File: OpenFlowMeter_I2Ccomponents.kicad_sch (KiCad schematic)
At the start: 7 parts, among them U7 24LC64, U9 TMP100

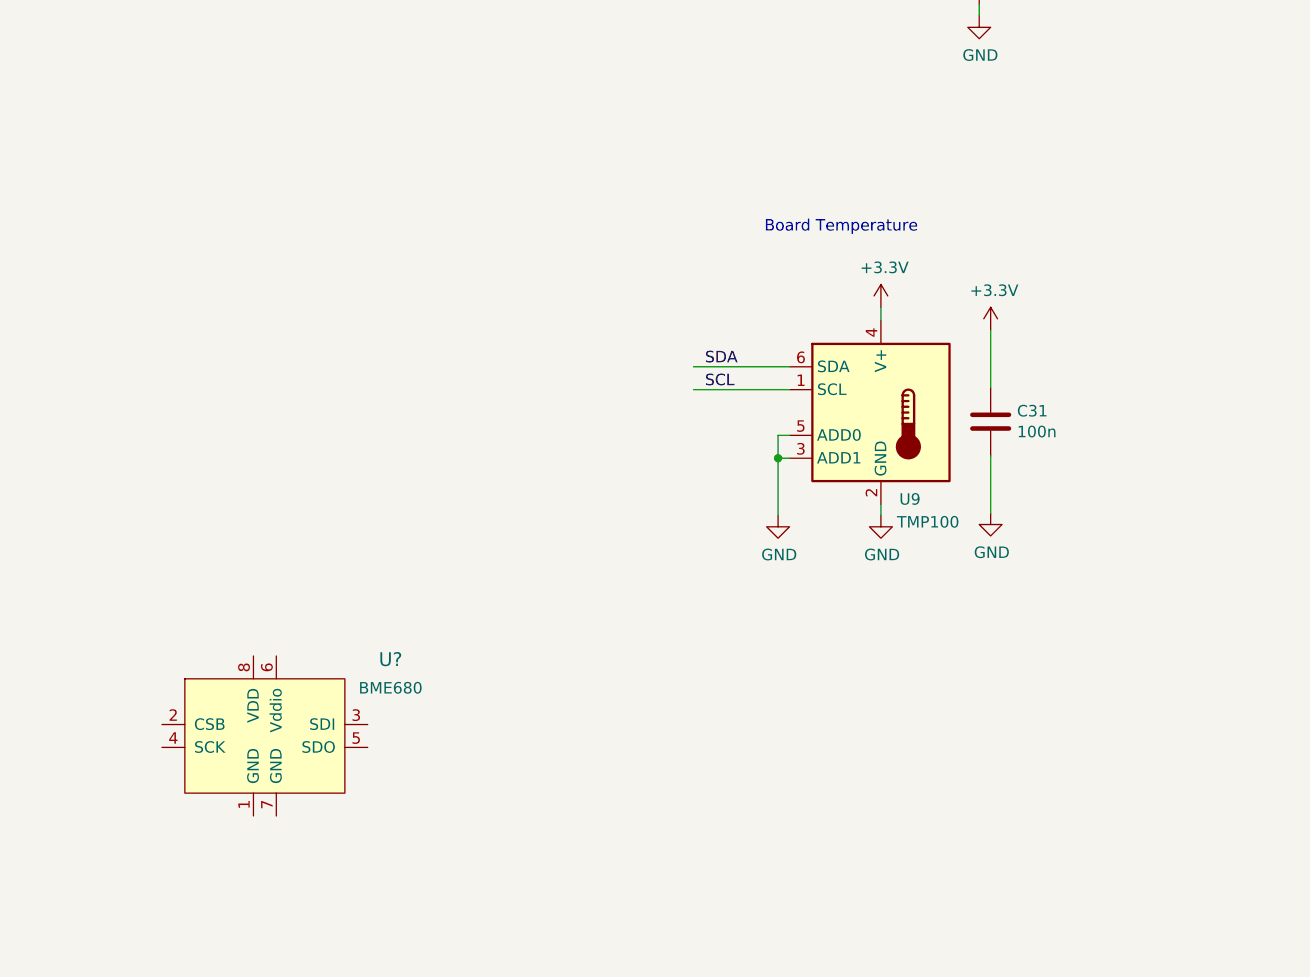
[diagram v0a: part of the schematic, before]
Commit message: added BME680 I2C sensor
Measurement of pressure / temperature and humidity and VOC. This might influence the flow and for ambient flow, this might be an option to measure and correct for them.
For measurements inside pipes, the gas through pipes are normally known and hence the correction should be known as well.
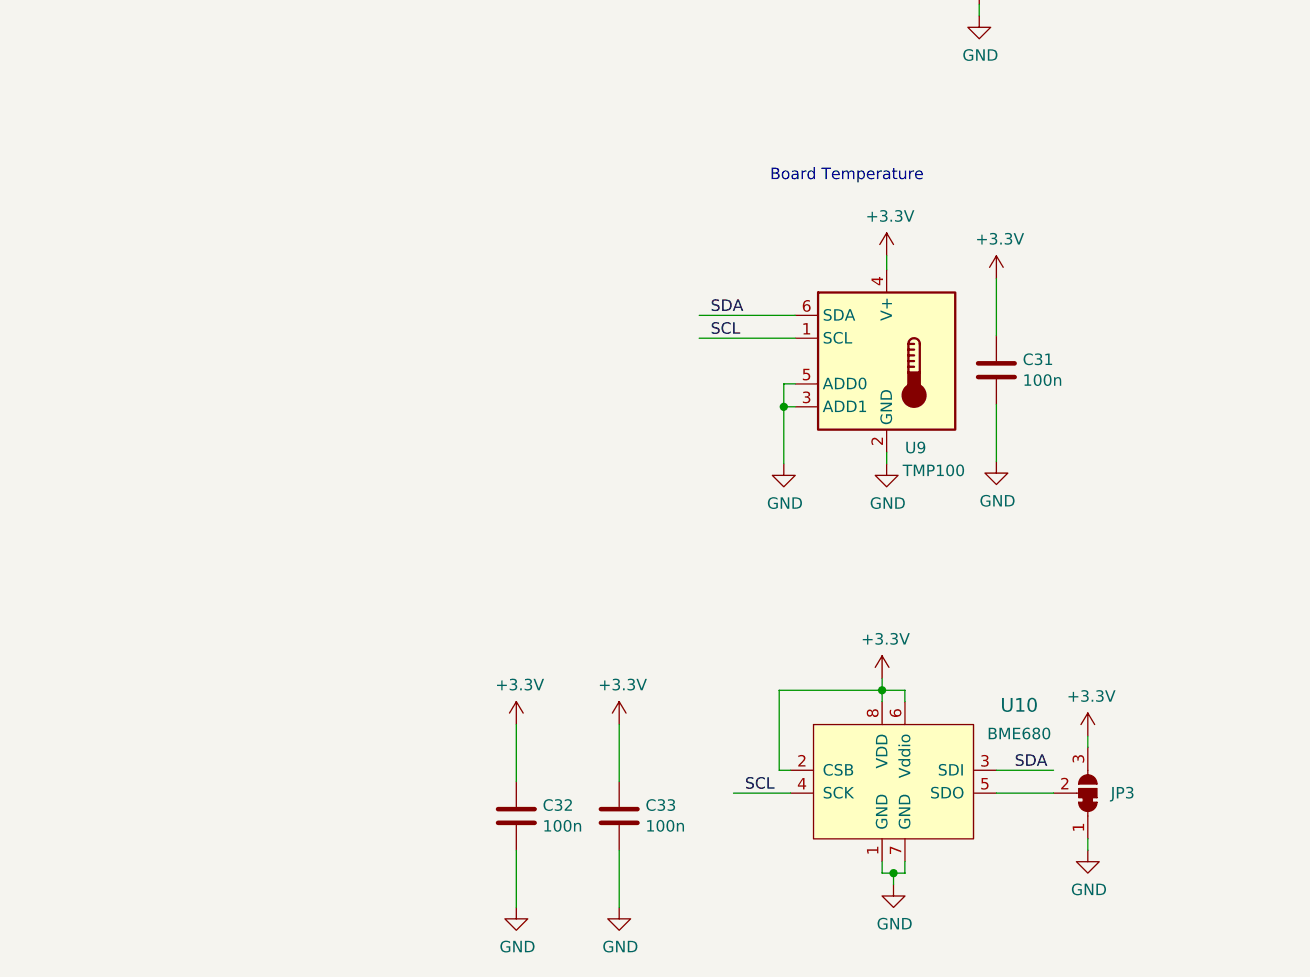
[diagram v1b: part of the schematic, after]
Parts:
- added C32, C33: 100n, Capacitor_SMD:C_0603_1608Metric, symbol Device:C
- added JP3: SolderJumper_3_Bridged12, Jumper:SolderJumper-3_P1.3mm_Bridged12_RoundedPad1.0x1.5mm, symbol Jumper:SolderJumper_3_Bridged12
- gave numbers to parts that had none: 1
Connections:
- net +3V3: now also U10.2 (CSB), U10.6 (Vddio), U10.8 (VDD), C32.1, C33.1, JP3.3 (B)
- net GND: now also U10.1 (GND), U10.7 (GND), C32.2, C33.2, JP3.1 (A)
- net SCL: now also U10.4 (SCK)
- net SDA: now also U10.3 (SDI)
- net at U10.5 (SDO): now also JP3.2 (C)
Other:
- moved on the sheet: C31, U10, U9
